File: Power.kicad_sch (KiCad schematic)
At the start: 60 parts, among them J7 XT60, J8 USB4105-GF-A, U14 LM217MDT-TR, U15 AP3211K, U16 INA3221, U17 LM217MDT-TR, U18 MIC2253, U19 LM217MDT-TR, U20 LM217MDT-TR, U21 USBLC6-4SC6

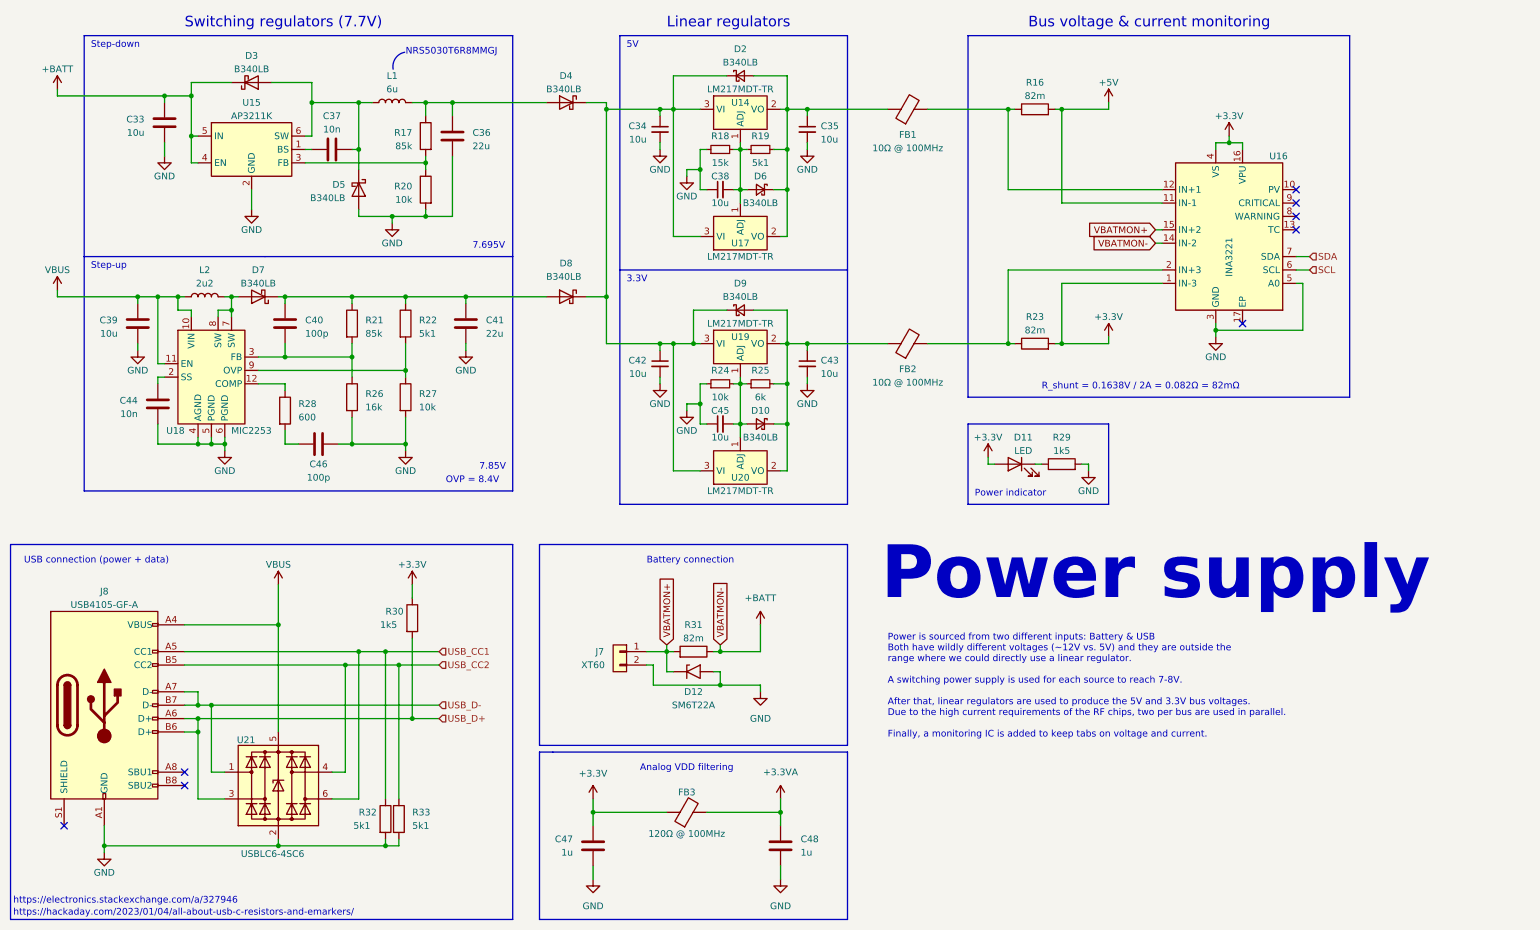
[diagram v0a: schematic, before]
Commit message: :building_construction: Simplify power circuit and consolidate BOM
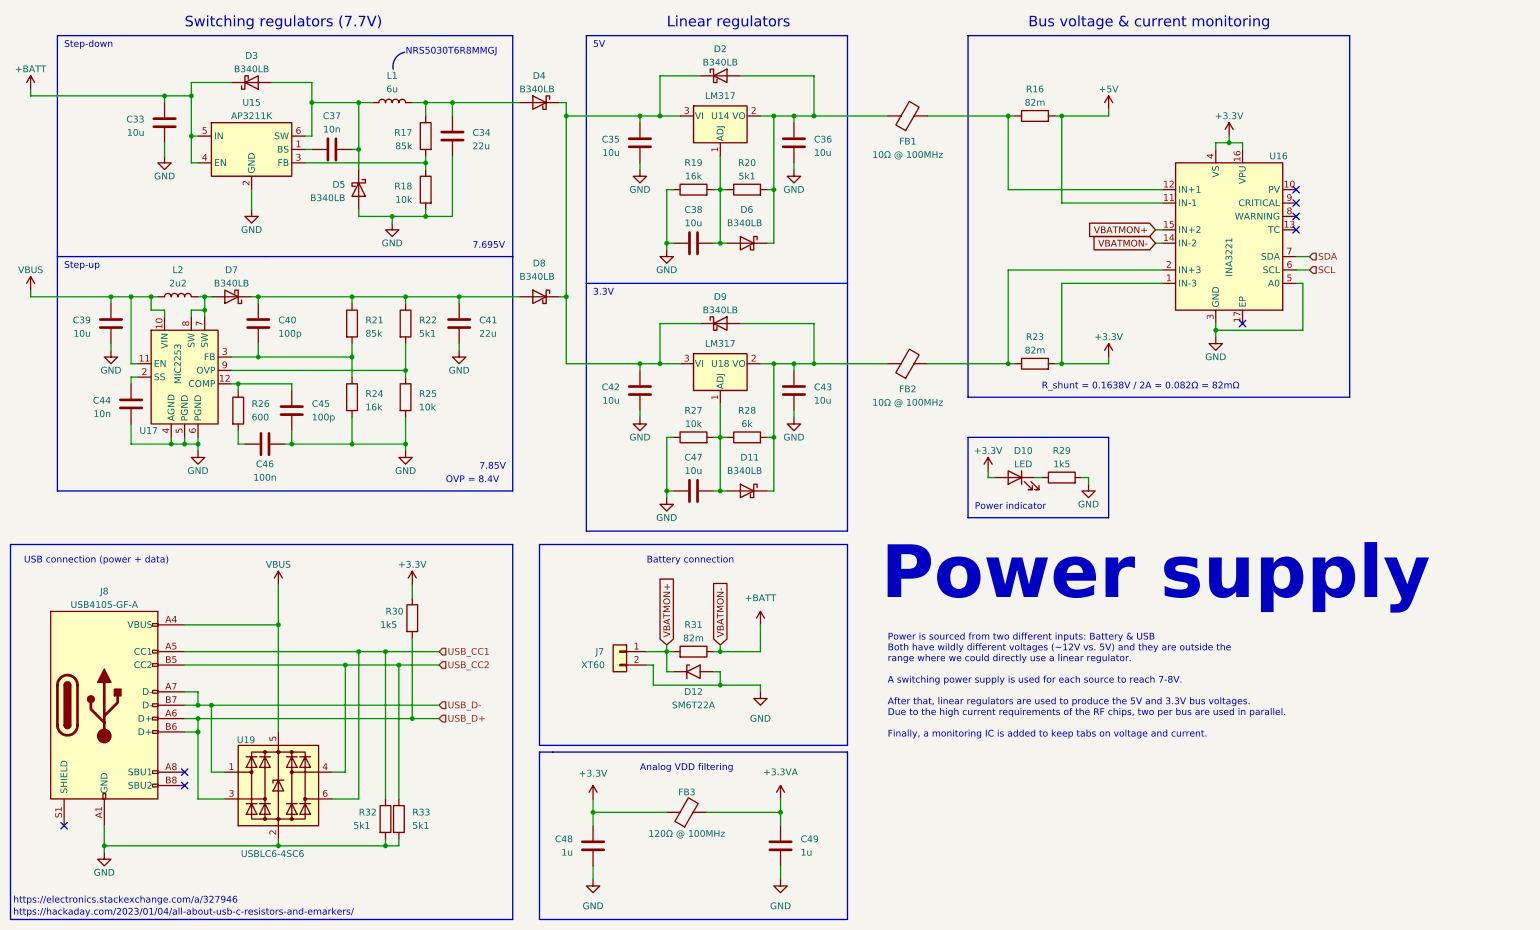
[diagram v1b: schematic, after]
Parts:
- removed C34, C35, C38, C42, C43, C45: 10u, Capacitor_SMD:C_0603_1608Metric_Pad1.08x0.95mm_HandSolder, symbol Device:C_Small
- removed D10, D2, D6, D9: B340LB, Diode_SMD:D_SMB_Handsoldering, symbol Device:D_Schottky_Small
- removed R18: 15k, Resistor_SMD:R_0402_1005Metric_Pad0.72x0.64mm_HandSolder, symbol Device:R_Small
- removed R19: 5k1, Resistor_SMD:R_0402_1005Metric_Pad0.72x0.64mm_HandSolder, symbol Device:R_Small
- removed R24: 10k, Resistor_SMD:R_0402_1005Metric_Pad0.72x0.64mm_HandSolder, symbol Device:R_Small
- removed R25: 6k, Resistor_SMD:R_0402_1005Metric_Pad0.72x0.64mm_HandSolder, symbol Device:R_Small
- removed U14, U17, U19, U20: LM217MDT-TR, Package_TO_SOT_SMD:TO-252-2, symbol Odyssey:LM217
- added C35, C36, C38, C42, C43, C47: 10u, Capacitor_SMD:C_0603_1608Metric_Pad1.08x0.95mm_HandSolder, symbol Device:C
- added C45: 100p, Capacitor_SMD:C_0402_1005Metric_Pad0.74x0.62mm_HandSolder, symbol Device:C
- added D11, D2, D6, D9: B340LB, Diode_SMD:D_SMB_Handsoldering, symbol Diode:1N5822
- added R19: 16k, Resistor_SMD:R_0402_1005Metric_Pad0.72x0.64mm_HandSolder, symbol Device:R
- added R20: 5k1, Resistor_SMD:R_0402_1005Metric_Pad0.72x0.64mm_HandSolder, symbol Device:R
- added R27: 10k, Resistor_SMD:R_0402_1005Metric_Pad0.72x0.64mm_HandSolder, symbol Device:R
- added R28: 6k, Resistor_SMD:R_0402_1005Metric_Pad0.72x0.64mm_HandSolder, symbol Device:R
- added U14, U18: LM317, Package_TO_SOT_SMD:TO-263-3_TabPin2, symbol Regulator_Linear:LM317_TO-263
- C46: value 100p -> 100n
- renumbered C36 to C34, C47 to C48, C48 to C49, D11 to D10, R20 to R18, R26 to R24, R27 to R25, R28 to R26, U18 to U17, U21 to U19
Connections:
- net GND: now also C35.2, C36.2, C38.1, C42.2, C43.2, C45.2, C47.1, R19.1, R27.1
- net at D4.1 (K), D8.1 (K): now also C35.1, C42.1, D2.1 (K), D9.1 (K), U14.3 (VI), U18.3 (VI)
- net at FB1.1: now also C36.1, D2.2 (A), D6.1 (K), R20.2, U14.2 (VO)
- net at R26.1, U17.12 (COMP): now also C45.1
- net at FB2.1: now also C43.1, D11.1 (K), D9.2 (A), R28.2, U18.2 (VO)
- new net: C38.2, D6.2 (A), R19.2, R20.1, U14.1 (ADJ)
- new net: C47.2, D11.2 (A), R27.2, R28.1, U18.1 (ADJ)
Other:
- moved on the sheet: C39, C40, C41, C44, C46, D10, D4, D7, D8, FB1, FB2, L2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

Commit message: :building_construction: Replace debug header with TagConnect and inline STM32 decoupling caps
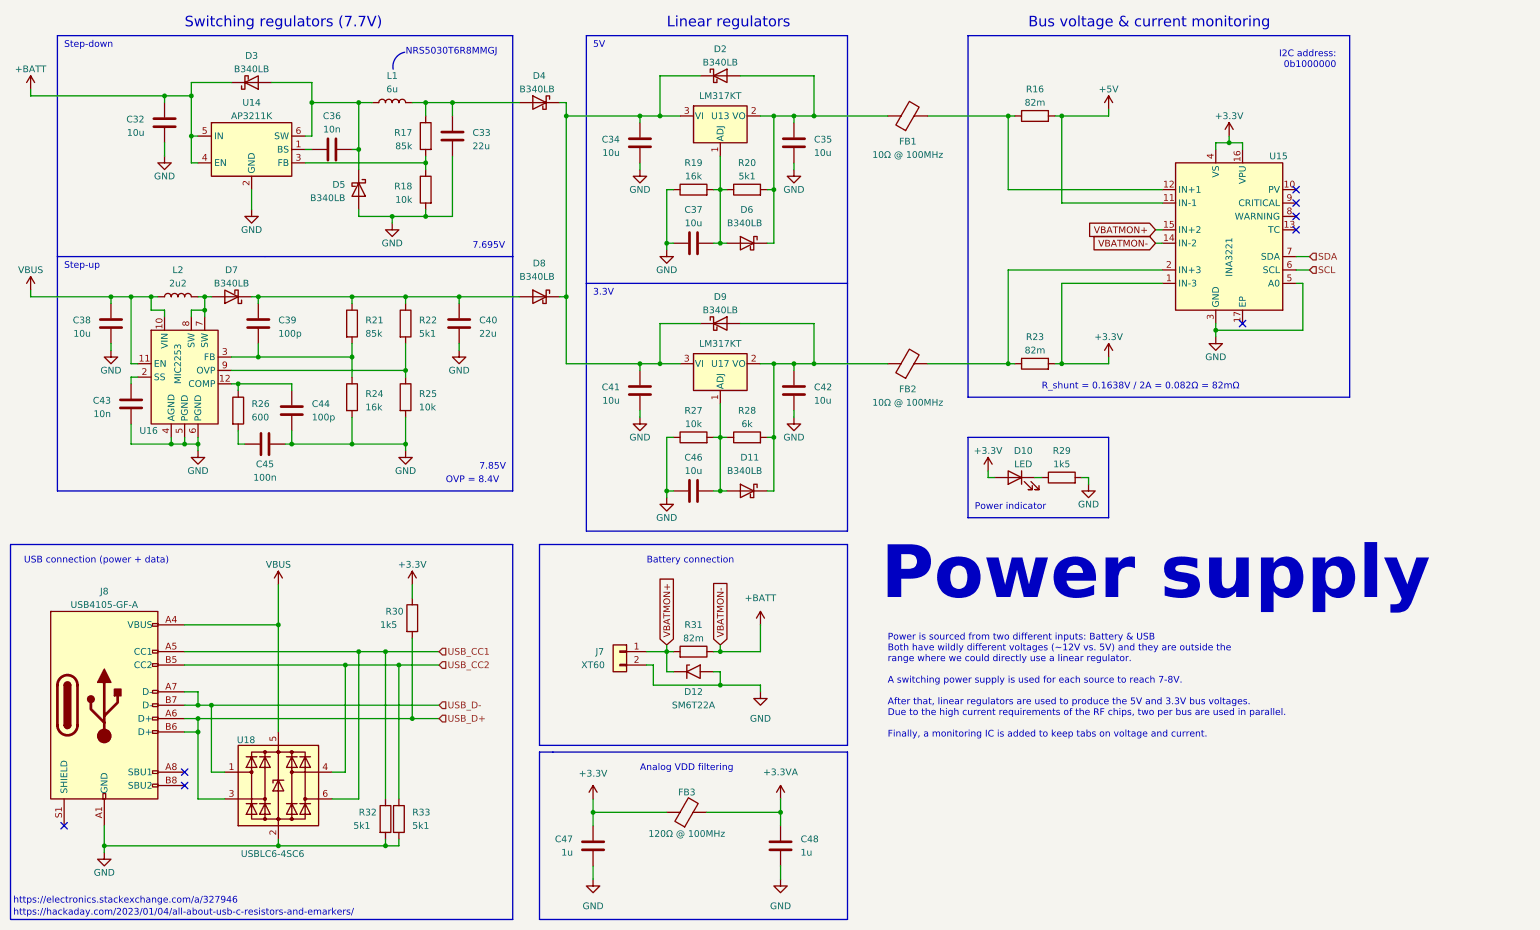
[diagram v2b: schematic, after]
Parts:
- U13: renamed from U14; value LM317 -> LM317KT
- U17: renamed from U18; value LM317 -> LM317KT
- renumbered C33 to C32, C34 to C33, C35 to C34, C36 to C35, C37 to C36, C38 to C37, C39 to C38, C40 to C39, C41 to C40, C42 to C41, C43 to C42, C44 to C43, C45 to C44, C46 to C45, C47 to C46, C48 to C47, C49 to C48, U15 to U14, U16 to U15, U17 to U16, U19 to U18
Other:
- note added: "I2C address: 0b1000000"

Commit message: :children_crossing: Add test pads and assign footprints
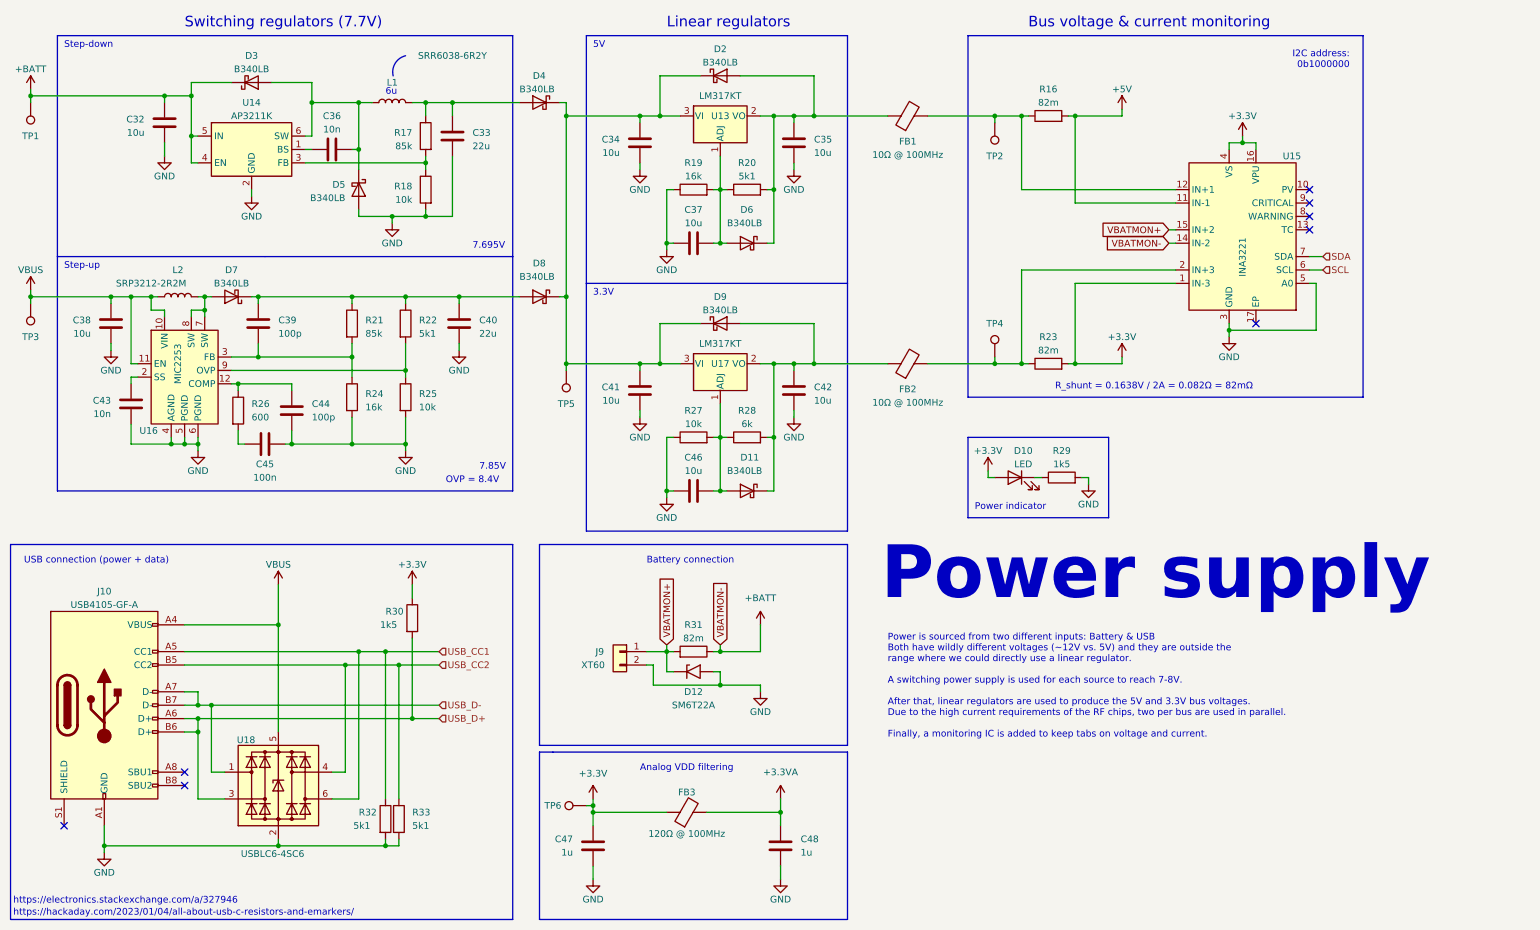
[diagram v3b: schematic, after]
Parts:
- added TP1, TP2, TP3, TP4, TP5, TP6: TestPoint, TestPoint:TestPoint_Pad_D2.0mm, symbol Connector:TestPoint
- J9: renamed from J7; footprint (none) -> Connector_AMASS:AMASS_XT60-M_1x02_P7.20mm_Vertical
- L1: value 6u -> SRR6038-6R2Y; footprint (none) -> Inductor_SMD:L_Bourns-SRR6038
- L2: value 2u2 -> SRP3212-2R2M; footprint (none) -> Inductor_SMD:L_1210_3225Metric
- renumbered J8 to J10
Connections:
- net +3.3V: now also TP6.1
- net +BATT: now also TP1.1
- net VBUS: now also TP3.1
- net at C34.1, C41.1, D2.1 (K)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: now also TP5.1
- net at FB1.2, R16.1, U15.12 (IN+1): now also TP2.1
- net at FB2.2, R23.1, U15.2 (IN+3): now also TP4.1
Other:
- note added: "6u"
- note removed: "NRS5030T6R8MMGJ"
- moved on the sheet: R16, R23, U15
